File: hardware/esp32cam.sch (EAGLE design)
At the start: 45 parts, among them J1 MICRO_USB_B_HIROSE_ZX62-B-5PA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, Q1 HN1C01FU, U1 NJM11100, U2 NJM11100, U3 FT234XD-R, U4 NJM12888F, U6 SPU0414HR5H-SB

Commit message: esp32cam途中
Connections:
- new net SPI0_CS: MICRO_SD.CD/DAT3
- new net SPI0_MISO: MICRO_SD.DAT0
- new net SPI0_MOSI: MICRO_SD.CMD
- new net SPI0_SCK: MICRO_SD.CLK
- net CAM_RESET: now also ESP32.IO6
- net D0: now also ESP32.IO39
- net D1: now also ESP32.IO41
- net D2: now also ESP32.IO42
- net D3: now also ESP32.IO40
- net D4: now also ESP32.IO38
- net D5: now also ESP32.IO35
- net D6: now also ESP32.IO45
- net D7: now also ESP32.IO47
- net HSYNC: now also ESP32.IO15
- net PCLK: now also ESP32.IO37
- net VSYNC: now also ESP32.IO7
- net XCLK: now also ESP32.IO48
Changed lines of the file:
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@@
 <pinref part="CAM" gate="G$1" pin="PCLK"/>
+</segment>
+<segment>
+<pinref part="ESP32" gate="G$1" pin="IO37"/>
+<wire x1="114.3" y1="104.14" x2="119.38" y2="104.14" width="0.1524" layer="91"/>
+<label x="119.38" y="104.14" size="1.778" layer="95" xref="yes"/>
 </segment>
 </net>
@@
 <pinref part="CAM" gate="G$1" pin="D2"/>
 </segment>
+<segment>
+<pinref part="ESP32" gate="G$1" pin="IO42"/>
+<wire x1="114.3" y1="91.44" x2="119.38" y2="91.44" width="0.1524" layer="91"/>
+<label x="119.38" y="91.44" size="1.778" layer="95" xref="yes"/>
+</segment>
 </net>
 <net name="D1" class="0">
@@
 <pinref part="CAM" gate="G$1" pin="D1"/>
 </segment>
+<segment>
+<pinref part="ESP32" gate="G$1" pin="IO41"/>
+<wire x1="114.3" y1="93.98" x2="119.38" y2="93.98" width="0.1524" layer="91"/>
+<label x="119.38" y="93.98" size="1.778" layer="95" xref="yes"/>
+</segment>
 </net>
 <net name="D0" class="0">
@@
 <pinref part="CAM" gate="G$1" pin="D0"/>
 </segment>
+<segment>
+<pinref part="ESP32" gate="G$1" pin="IO39"/>
+<wire x1="114.3" y1="99.06" x2="119.38" y2="99.06" width="0.1524" layer="91"/>
+<label x="119.38" y="99.06" size="1.778" layer="95" xref="yes"/>
+</segment>
 </net>
 <net name="D3" class="0">
@@
 <pinref part="CAM" gate="G$1" pin="D3"/>
 </segment>
+<segment>
+<pinref part="ESP32" gate="G$1" pin="IO40"/>
+<wire x1="114.3" y1="96.52" x2="119.38" y2="96.52" width="0.1524" layer="91"/>
+<label x="119.38" y="96.52" size="1.778" layer="95" xref="yes"/>
+</segment>
 </net>
 <net name="D4" class="0">
@@
 <pinref part="CAM" gate="G$1" pin="D4"/>
 </segment>
+<segment>
+<pinref part="ESP32" gate="G$1" pin="IO38"/>
+<wire x1="114.3" y1="101.6" x2="119.38" y2="101.6" width="0.1524" layer="91"/>
+<label x="119.38" y="101.6" size="1.778" layer="95" xref="yes"/>
+</segment>
 </net>
 <net name="D5" class="0">
@@
 <pinref part="CAM" gate="G$1" pin="D5"/>
 </segment>
+<segment>
+<pinref part="ESP32" gate="G$1" pin="IO35"/>
+<wire x1="114.3" y1="109.22" x2="119.38" y2="109.22" width="0.1524" layer="91"/>
+<label x="119.38" y="109.22" size="1.778" layer="95" xref="yes"/>
+</segment>
 </net>
 <net name="D6" class="0">
@@
 <pinref part="CAM" gate="G$1" pin="D6"/>
 </segment>
+<segment>
+<pinref part="ESP32" gate="G$1" pin="IO45"/>
+<wire x1="114.3" y1="88.9" x2="119.38" y2="88.9" width="0.1524" layer="91"/>
+<label x="119.38" y="88.9" size="1.778" layer="95" xref="yes"/>
+</segment>
 </net>
 <net name="D7" class="0">
@@
 <pinref part="CAM" gate="G$1" pin="D7"/>
 </segment>
+<segment>
+<pinref part="ESP32" gate="G$1" pin="IO47"/>
+<wire x1="114.3" y1="83.82" x2="119.38" y2="83.82" width="0.1524" layer="91"/>
+<label x="119.38" y="83.82" size="1.778" layer="95" xref="yes"/>
+</segment>
 </net>
 <net name="CAM_RESET" class="0">
@@
 <pinref part="CAM" gate="G$1" pin="RST"/>
 </segment>
+<segment>
+<pinref part="ESP32" gate="G$1" pin="IO6"/>
+<wire x1="83.82" y1="106.68" x2="81.28" y2="106.68" width="0.1524" layer="91"/>
+<label x="81.28" y="106.68" size="1.778" layer="95" rot="R180" xref="yes"/>
+</segment>
 </net>
 <net name="VSYNC" class="0">
@@
 <pinref part="CAM" gate="G$1" pin="VSYNC"/>
 </segment>
+<segment>
+<pinref part="ESP32" gate="G$1" pin="IO7"/>
+<wire x1="83.82" y1="104.14" x2="81.28" y2="104.14" width="0.1524" layer="91"/>
+<label x="81.28" y="104.14" size="1.778" layer="95" rot="R180" xref="yes"/>
+</segment>
 </net>
 <net name="N$10" class="0">
@@
 <pinref part="CAM" gate="G$1" pin="HREF"/>
 </segment>
+<segment>
+<pinref part="ESP32" gate="G$1" pin="IO15"/>
+<wire x1="83.82" y1="83.82" x2="78.74" y2="83.82" width="0.1524" layer="91"/>
+<label x="78.74" y="83.82" size="1.778" layer="95" rot="R180" xref="yes"/>
+</segment>
 </net>
 <net name="XCLK" class="0">
@@
 <label x="81.28" y="20.32" size="1.778" layer="95" xref="yes"/>
 <pinref part="CAM" gate="G$1" pin="XCLK"/>
+</segment>
+<segment>
+<pinref part="ESP32" gate="G$1" pin="IO48"/>
+<wire x1="114.3" y1="81.28" x2="119.38" y2="81.28" width="0.1524" layer="91"/>
+<label x="119.38" y="81.28" size="1.778" layer="95" xref="yes"/>
 </segment>
 </net>
@@
 </segment>
 </net>
+<net name="SPI0_MISO" class="0">
+<segment>
+<pinref part="MICRO_SD" gate="G$1" pin="DAT0"/>
+<wire x1="215.9" y1="129.54" x2="210.82" y2="129.54" width="0.1524" layer="91"/>
+<label x="210.82" y="129.54" size="1.778" layer="95"/>
+</segment>
+</net>
+<net name="SPI0_CS" class="0">
+<segment>
+<pinref part="MICRO_SD" gate="G$1" pin="CD/DAT3"/>
+<wire x1="215.9" y1="121.92" x2="210.82" y2="121.92" width="0.1524" layer="91"/>
+<label x="210.82" y="121.92" size="1.778" layer="95"/>
+</segment>
+</net>
+<net name="SPI0_MOSI" class="0">
+<segment>
+<pinref part="MICRO_SD" gate="G$1" pin="CMD"/>
+<wire x1="215.9" y1="119.38" x2="210.82" y2="119.38" width="0.1524" layer="91"/>
+<label x="210.82" y="119.38" size="1.778" layer="95"/>
+</segment>
+</net>
+<net name="SPI0_SCK" class="0">
+<segment>
+<pinref part="MICRO_SD" gate="G$1" pin="CLK"/>
+<wire x1="215.9" y1="116.84" x2="210.82" y2="116.84" width="0.1524" layer="91"/>
+<label x="210.82" y="116.84" size="1.778" layer="95"/>
+</segment>
+</net>

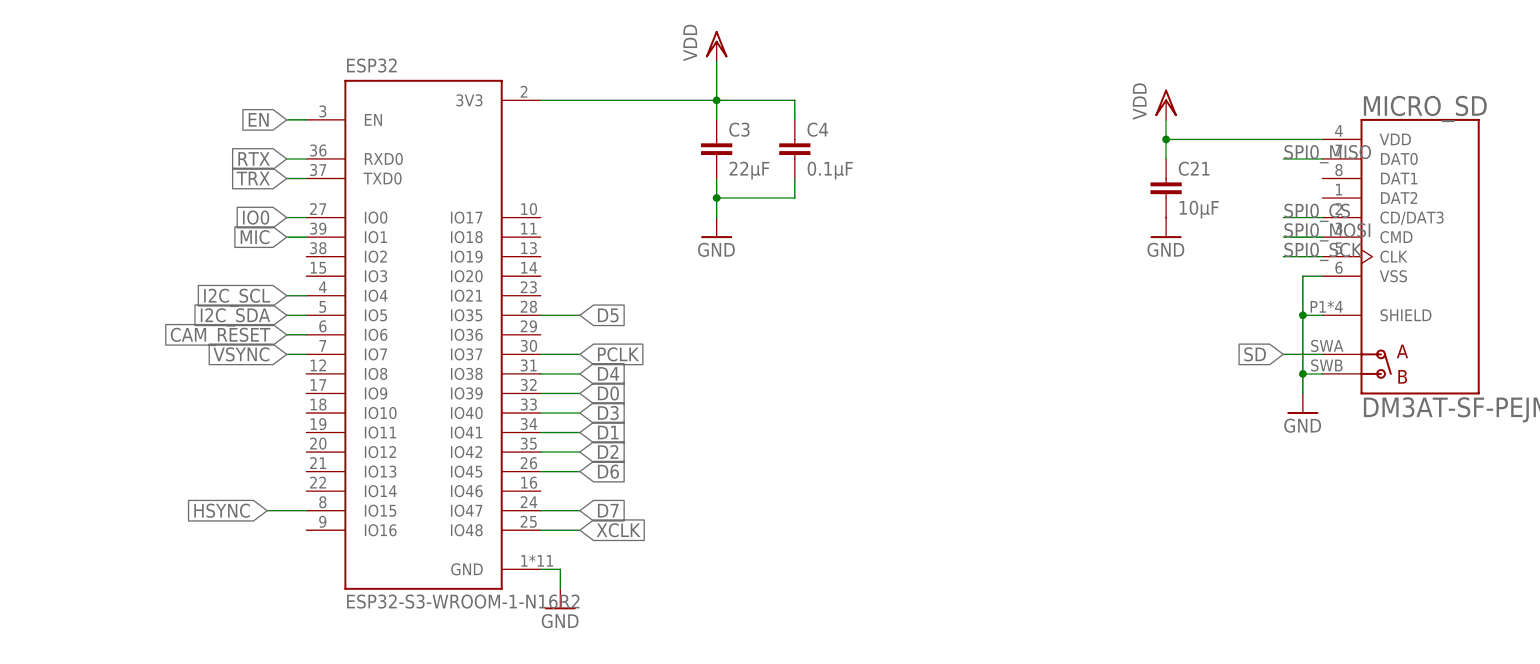
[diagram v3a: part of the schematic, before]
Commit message: 変更点:カメラモジュール・SDカード・LED1,2接続、未接続だったVDD、GNDの接続 一応完成したはずです。確認お願いします。
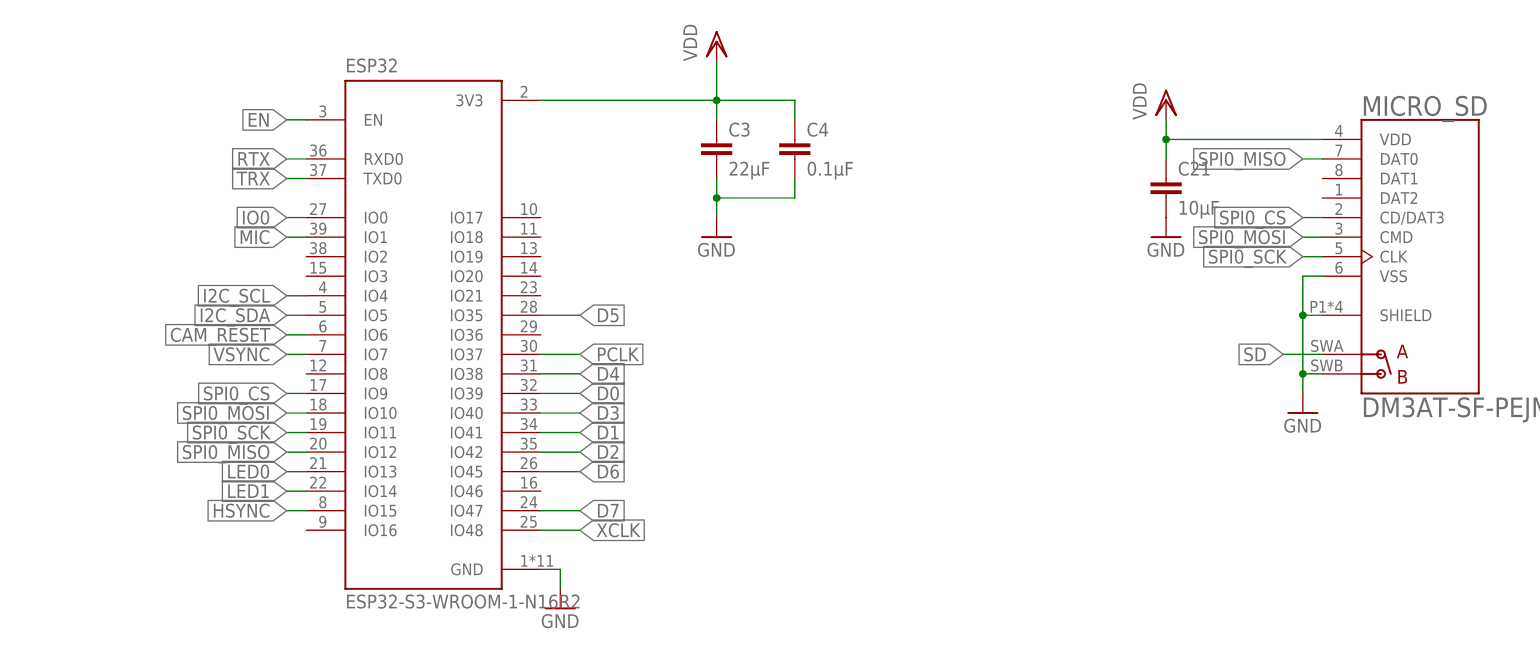
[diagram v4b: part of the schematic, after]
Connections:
- net LED0: now also ESP32.IO13
- net LED1: now also ESP32.IO14
- net SPI0_CS: now also ESP32.IO9
- net SPI0_MISO: now also ESP32.IO12
- net SPI0_MOSI: now also ESP32.IO10
- net SPI0_SCK: now also ESP32.IO11
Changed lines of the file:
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@@
 <label x="-25.4" y="88.9" size="1.778" layer="95" rot="R90" xref="yes"/>
+</segment>
+<segment>
+<pinref part="ESP32" gate="G$1" pin="IO13"/>
+<wire x1="83.82" y1="88.9" x2="81.28" y2="88.9" width="0.1524" layer="91"/>
+<label x="81.28" y="88.9" size="1.778" layer="95" rot="R180" xref="yes"/>
 </segment>
 </net>
@@
 <wire x1="-15.24" y1="86.36" x2="-15.24" y2="88.9" width="0.1524" layer="91"/>
 <label x="-15.24" y="88.9" size="1.778" layer="95" rot="R90" xref="yes"/>
+</segment>
+<segment>
+<pinref part="ESP32" gate="G$1" pin="IO14"/>
+<wire x1="83.82" y1="86.36" x2="81.28" y2="86.36" width="0.1524" layer="91"/>
+<label x="81.28" y="86.36" size="1.778" layer="95" rot="R180" xref="yes"/>
 </segment>
 </net>
@@
 <segment>
 <pinref part="ESP32" gate="G$1" pin="IO15"/>
-<wire x1="83.82" y1="83.82" x2="78.74" y2="83.82" width="0.1524" layer="91"/>
-<label x="78.74" y="83.82" size="1.778" layer="95" rot="R180" xref="yes"/>
+<wire x1="83.82" y1="83.82" x2="81.28" y2="83.82" width="0.1524" layer="91"/>
+<label x="81.28" y="83.82" size="1.778" layer="95" rot="R180" xref="yes"/>
 </segment>
 </net>
@@
 <segment>
 <pinref part="MICRO_SD" gate="G$1" pin="DAT0"/>
-<wire x1="215.9" y1="129.54" x2="210.82" y2="129.54" width="0.1524" layer="91"/>
-<label x="210.82" y="129.54" size="1.778" layer="95"/>
+<wire x1="215.9" y1="129.54" x2="213.36" y2="129.54" width="0.1524" layer="91"/>
+<label x="213.36" y="129.54" size="1.778" layer="95" rot="R180" xref="yes"/>
+</segment>
+<segment>
+<pinref part="ESP32" gate="G$1" pin="IO12"/>
+<wire x1="83.82" y1="91.44" x2="81.28" y2="91.44" width="0.1524" layer="91"/>
+<label x="81.28" y="91.44" size="1.778" layer="95" rot="R180" xref="yes"/>
 </segment>
 </net>
@@
 <segment>
 <pinref part="MICRO_SD" gate="G$1" pin="CD/DAT3"/>
-<wire x1="215.9" y1="121.92" x2="210.82" y2="121.92" width="0.1524" layer="91"/>
-<label x="210.82" y="121.92" size="1.778" layer="95"/>
+<wire x1="215.9" y1="121.92" x2="213.36" y2="121.92" width="0.1524" layer="91"/>
+<label x="213.36" y="121.92" size="1.778" layer="95" rot="R180" xref="yes"/>
+</segment>
+<segment>
+<pinref part="ESP32" gate="G$1" pin="IO9"/>
+<wire x1="83.82" y1="99.06" x2="81.28" y2="99.06" width="0.1524" layer="91"/>
+<label x="81.28" y="99.06" size="1.778" layer="95" rot="R180" xref="yes"/>
 </segment>
 </net>
@@
 <segment>
 <pinref part="MICRO_SD" gate="G$1" pin="CMD"/>
-<wire x1="215.9" y1="119.38" x2="210.82" y2="119.38" width="0.1524" layer="91"/>
-<label x="210.82" y="119.38" size="1.778" layer="95"/>
+<wire x1="215.9" y1="119.38" x2="213.36" y2="119.38" width="0.1524" layer="91"/>
+<label x="213.36" y="119.38" size="1.778" layer="95" rot="R180" xref="yes"/>
+</segment>
+<segment>
+<pinref part="ESP32" gate="G$1" pin="IO10"/>
+<wire x1="83.82" y1="96.52" x2="81.28" y2="96.52" width="0.1524" layer="91"/>
+<label x="81.28" y="96.52" size="1.778" layer="95" rot="R180" xref="yes"/>
 </segment>
 </net>
@@
 <segment>
 <pinref part="MICRO_SD" gate="G$1" pin="CLK"/>
-<wire x1="215.9" y1="116.84" x2="210.82" y2="116.84" width="0.1524" layer="91"/>
-<label x="210.82" y="116.84" size="1.778" layer="95"/>
+<wire x1="215.9" y1="116.84" x2="213.36" y2="116.84" width="0.1524" layer="91"/>
+<label x="213.36" y="116.84" size="1.778" layer="95" rot="R180" xref="yes"/>
+</segment>
+<segment>
+<pinref part="ESP32" gate="G$1" pin="IO11"/>
+<wire x1="83.82" y1="93.98" x2="81.28" y2="93.98" width="0.1524" layer="91"/>
+<label x="81.28" y="93.98" size="1.778" layer="95" rot="R180" xref="yes"/>
 </segment>
 </net>
@@
 </sheet>
 </sheets>
+<errors>
+</errors>
 </schematic>
 </drawing>

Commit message: 若干修正
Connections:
- net RX0: now also ESP32.IO36
- net RX1: now also ESP32.IO17
- net SD: now also ESP32.IO21
- net TX0: now also ESP32.IO2
- net TX1: now also ESP32.IO16
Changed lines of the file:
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@@
 <pinref part="C9" gate="G$1" pin="4"/>
+</segment>
+<segment>
+<pinref part="ESP32" gate="G$1" pin="IO36"/>
+<wire x1="114.3" y1="106.68" x2="119.38" y2="106.68" width="0.1524" layer="91"/>
+<label x="119.38" y="106.68" size="1.778" layer="95" xref="yes"/>
 </segment>
 </net>
@@
 <pinref part="C9" gate="G$1" pin="2"/>
 </segment>
+<segment>
+<pinref part="ESP32" gate="G$1" pin="IO2"/>
+<wire x1="81.28" y1="116.84" x2="83.82" y2="116.84" width="0.1524" layer="91"/>
+<label x="81.28" y="116.84" size="1.778" layer="95" rot="R180" xref="yes"/>
+</segment>
 </net>
 <net name="RX1" class="0">
@@
 <wire x1="99.06" y1="185.42" x2="91.44" y2="185.42" width="0.1524" layer="91"/>
 </segment>
+<segment>
+<pinref part="ESP32" gate="G$1" pin="IO17"/>
+<wire x1="114.3" y1="121.92" x2="116.84" y2="121.92" width="0.1524" layer="91"/>
+<label x="116.84" y="121.92" size="1.778" layer="95" xref="yes"/>
+</segment>
 </net>
 <net name="TX1" class="0">
@@
 <pinref part="C10" gate="G$1" pin="2"/>
 <wire x1="99.06" y1="190.5" x2="91.44" y2="190.5" width="0.1524" layer="91"/>
+</segment>
+<segment>
+<pinref part="ESP32" gate="G$1" pin="IO16"/>
+<wire x1="83.82" y1="81.28" x2="81.28" y2="81.28" width="0.1524" layer="91"/>
+<label x="81.28" y="81.28" size="1.778" layer="95" rot="R180" xref="yes"/>
 </segment>
 </net>
@@
 <label x="210.82" y="104.14" size="1.778" layer="95" rot="R180" xref="yes"/>
 </segment>
-</net>
+<segment>
+<pinref part="ESP32" gate="G$1" pin="IO21"/>
+<wire x1="114.3" y1="111.76" x2="119.38" y2="111.76" width="0.1524" layer="91"/>
+<label x="119.38" y="111.76" size="1.778" layer="95" xref="yes"/>
+</segment>
+</net>

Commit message: 回路微修正
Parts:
- removed C5: 0.1µF, rcl:C-EUC0402
- removed U3: FT234XD-R, FT234XD-R:FT234XD-R
- added C22: 1µF, rcl:C-EUC0402
- added PROG, RESET: THAF01-NC-R, switches:THAF01-NC-R
- R1, R2: value (none) -> 1k
- VR1, VR2: value (none) -> 100k
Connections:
- net 1.3V renamed 1.5V
- removed net DTR: Q1G$2.E, R3.1
- removed net N$6: C5.1, U3.!RESET#, U3.3V3OUT, U3.VCCIO
- removed net RTS: Q1G$1.E, R4.1, U3.RTS#
- removed net RTX: ESP32.RXD0, U3.TXD
- removed net TRX: ESP32.TXD0, U3.RXD
- new net CAM_POWER: ESP32.TXD0, U1.CONTROL, U2.CONTROL
- new net N$5: PROG.B, R3.1, R4.1
- new net SDIO_D1: ESP32.IO8, MICRO_SD.DAT1
- new net SDIO_D2: ESP32.IO18, MICRO_SD.DAT2
- net D5: now also ESP32.IO46; no longer ESP32.IO35
- net EN: now also RESET.B
- net GND: now also C22.2, Q1G$1.E, Q1G$2.E, RESET.A; no longer C5.2, U3.GND
- net IO0: now also C22.1
- net PCLK: now also ESP32.IO3; no longer ESP32.IO37
- net RX0: now also ESP32.RXD0; no longer ESP32.IO36
- net USB_DM: now also ESP32.IO19; no longer U3.USBDM
- net USB_DP: now also ESP32.IO20; no longer U3.USBDP
- net USB_VCC: no longer U3.VCC
- net V+: now also C13.1, C7.1, U1.VIN, U2.VIN
- net VDD: now also PROG.A; no longer C13.1, C7.1, U1.CONTROL, U1.VIN, U2.CONTROL, U2.VIN
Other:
- moved on the sheet: C11, C12, C13, C14, C15, C16, C21, C6, C7, C8, LED0, LED1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
